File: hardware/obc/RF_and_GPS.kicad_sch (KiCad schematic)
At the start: 15 parts, among them J602 SMA RA Connector, J603 SMA RA Connector, J604 SMA RA Connector, U102 BMI088, U601 RFM98PW, U602 S1216V8, U603 GP2S1+

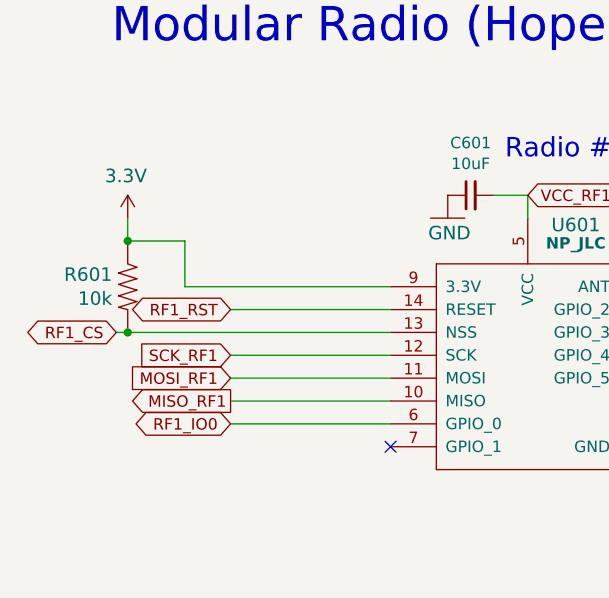
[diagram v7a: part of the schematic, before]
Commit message: OBC: Continuing work towards the next revision
- Cleaned up text on Avionics Page
- Changed some descriptions and cleaned up text on Power Page
- Changed Power Relay A schematic to one from PCB
- Changed R120 and R401 changed from 107k to 34.8k and changed R121 and R404 from 0 to 10k and R127 and R419 from 3.01k to 3.83k (Solar Chargers Page)
- Checked R303 and R304 resistor value and believe 27 is correct
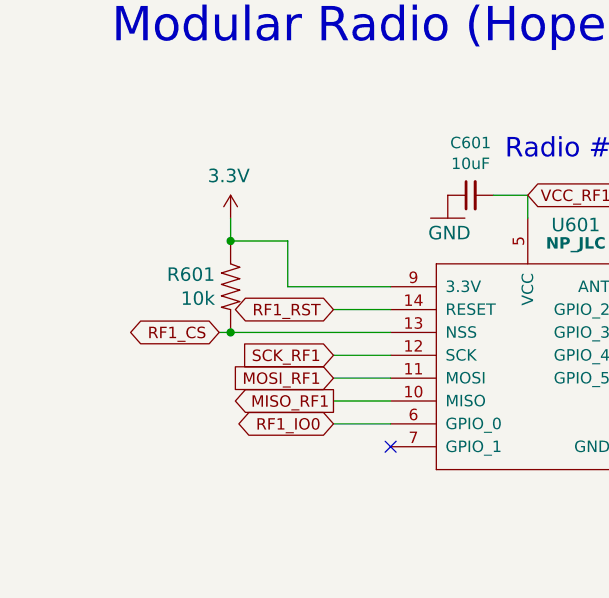
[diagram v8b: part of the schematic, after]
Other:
- moved on the sheet: R601
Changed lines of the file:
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@@
 	)
 	(junction
-		(at 41.91 53.34)
+		(at 53.34 53.34)
 		(diameter 0)
 		(color 0 0 0 0)
@@
 	)
 	(junction
-		(at 41.91 63.5)
+		(at 53.34 63.5)
 		(diameter 0)
 		(color 0 0 0 0)
@@
 	(wire
 		(pts
-			(xy 40.64 63.5) (xy 41.91 63.5)
+			(xy 52.07 63.5) (xy 53.34 63.5)
 		)
 		(stroke
@@
 	(wire
 		(pts
-			(xy 71.12 58.42) (xy 48.26 58.42)
+			(xy 71.12 58.42) (xy 59.69 58.42)
 		)
 		(stroke
@@
 	(wire
 		(pts
-			(xy 48.26 53.34) (xy 41.91 53.34)
-		)
-		(stroke
-			(width 0)
-			(type default)
-		)
-	)
-	(wire
-		(pts
-			(xy 71.12 68.58) (xy 53.34 68.58)
+			(xy 59.69 53.34) (xy 53.34 53.34)
+		)
+		(stroke
+			(width 0)
+			(type default)
+		)
+	)
+	(wire
+		(pts
+			(xy 71.12 68.58) (xy 64.77 68.58)
 		)
 		(stroke
@@
 	(wire
 		(pts
-			(xy 48.26 58.42) (xy 48.26 53.34)
-		)
-		(stroke
-			(width 0)
-			(type default)
-		)
-	)
-	(wire
-		(pts
-			(xy 71.12 71.12) (xy 53.34 71.12)
+			(xy 59.69 58.42) (xy 59.69 53.34)
+		)
+		(stroke
+			(width 0)
+			(type default)
+		)
+	)
+	(wire
+		(pts
+			(xy 71.12 71.12) (xy 64.77 71.12)
 		)
 		(stroke
@@
 	(wire
 		(pts
-			(xy 71.12 60.96) (xy 53.34 60.96)
+			(xy 71.12 60.96) (xy 64.77 60.96)
 		)
 		(stroke
@@
 	(wire
 		(pts
-			(xy 41.91 53.34) (xy 41.91 50.8)
+			(xy 53.34 53.34) (xy 53.34 50.8)
 		)
 		(stroke
@@
 	(wire
 		(pts
-			(xy 41.91 63.5) (xy 71.12 63.5)
+			(xy 53.34 63.5) (xy 71.12 63.5)
 		)
 		(stroke
@@
 	(wire
 		(pts
-			(xy 71.12 66.04) (xy 53.34 66.04)
+			(xy 71.12 66.04) (xy 64.77 66.04)
 		)
 		(stroke
@@
 	(wire
 		(pts
-			(xy 53.34 73.66) (xy 71.12 73.66)
+			(xy 64.77 73.66) (xy 71.12 73.66)
 		)
 		(stroke
@@
 	(global_label "RF1_RST"
 		(shape bidirectional)
-		(at 53.34 60.96 180)
+		(at 64.77 60.96 180)
 		(effects
 			(font
@@
 		)
 		(property "Intersheetrefs" "${INTERSHEET_REFS}"
-			(at 53.34 60.96 0)
+			(at 64.77 60.96 0)
 			(effects
 				(font
@@
 	(global_label "RF1_IO0"
 		(shape bidirectional)
-		(at 53.34 73.66 180)
+		(at 64.77 73.66 180)
 		(effects
 			(font
@@
 		)
 		(property "Intersheetrefs" "${INTERSHEET_REFS}"
-			(at 53.34 73.66 0)
+			(at 64.77 73.66 0)
 			(effects
 				(font
@@
 	(global_label "MOSI_RF1"
 		(shape input)
-		(at 53.34 68.58 180)
+		(at 64.77 68.58 180)
 		(effects
 			(font
@@
 		)
 		(property "Intersheetrefs" "${INTERSHEET_REFS}"
-			(at 53.34 68.58 0)
+			(at 64.77 68.58 0)
 			(effects
 				(font
@@
 	(global_label "RF1_CS"
 		(shape bidirectional)
-		(at 40.64 63.5 180)
+		(at 52.07 63.5 180)
 		(effects
 			(font
@@
 		)
 		(property "Intersheetrefs" "${INTERSHEET_REFS}"
-			(at 40.64 63.5 0)
+			(at 52.07 63.5 0)
 			(effects
 				(font
@@
 	(global_label "SCK_RF1"
 		(shape input)
-		(at 53.34 66.04 180)
+		(at 64.77 66.04 180)
 		(effects
 			(font
@@
 		)
 		(property "Intersheetrefs" "${INTERSHEET_REFS}"
-			(at 53.34 66.04 0)
+			(at 64.77 66.04 0)
 			(effects
 				(font
@@
 	(global_label "MISO_RF1"
 		(shape output)
-		(at 53.34 71.12 180)
+		(at 64.77 71.12 180)
 		(effects
 			(font
@@
 		)
 		(property "Intersheetrefs" "${INTERSHEET_REFS}"
-			(at 53.34 71.12 0)
+			(at 64.77 71.12 0)
 			(effects
 				(font
@@
 	(symbol
 		(lib_id "mainboard:10KOHM-1_10W-1%(0603)0603")
-		(at 41.91 58.42 270)
+		(at 53.34 58.42 270)
 		(unit 1)
 		(exclude_from_sim no)
@@
 		(dnp no)
 		(property "Reference" "R601"
-			(at 40.1828 57.0738 90)
+			(at 51.6128 57.0738 90)
 			(effects
 				(font
@@
 		)
 		(property "Value" "10k"
-			(at 40.1828 59.7408 90)
+			(at 51.6128 59.7408 90)
 			(effects
 				(font
@@
 		)
 		(property "Footprint" "Resistor_SMD:R_0603_1608Metric"
-			(at 41.91 58.42 0)
+			(at 53.34 58.42 0)
 			(effects
 				(font
@@
 		)
 		(property "Datasheet" ""
-			(at 41.91 58.42 0)
+			(at 53.34 58.42 0)
 			(effects
 				(font
@@
 		)
 		(property "Description" "10k 0603"
-			(at 42.7228 57.0738 0)
+			(at 54.1528 57.0738 0)
 			(effects
 				(font
@@
 		)
 		(property "LCSC" "C169849"
-			(at 41.91 58.42 0)
+			(at 53.34 58.42 0)
 			(effects
 				(font
@@
 		)
 		(property "Notes" ""
-			(at 41.91 58.42 0)
+			(at 53.34 58.42 0)
 			(effects
 				(font
@@
 		)
 		(property "Manufacturer_Name" "PANASONIC"
-			(at 41.91 58.42 0)
+			(at 53.34 58.42 0)
 			(effects
 				(font
@@
 		)
 		(property "Manufacturer_Part_Number" "ERJ3GEYJ103V"
-			(at 41.91 58.42 0)
+			(at 53.34 58.42 0)
 			(effects
 				(font
@@
 		)
 		(property "Height" ""
-			(at 41.91 58.42 0)
+			(at 53.34 58.42 0)
 			(effects
 				(font
@@
 		)
 		(property "Mouser Part Number" ""
-			(at 41.91 58.42 0)
+			(at 53.34 58.42 0)
 			(effects
 				(font
@@
 		)
 		(property "Mouser Price/Stock" ""
-			(at 41.91 58.42 0)
+			(at 53.34 58.42 0)
 			(effects
 				(font
@@
 	(symbol
 		(lib_id "mainboard:3.3V")
-		(at 41.91 50.8 0)
+		(at 53.34 50.8 0)
 		(unit 1)
 		(exclude_from_sim no)
@@
 		(dnp no)
 		(property "Reference" "#SUPPLY0601"
-			(at 41.91 50.8 0)
+			(at 53.34 50.8 0)
 			(effects
 				(font
@@
 		)
 		(property "Value" "3.3V"
-			(at 39.37 46.99 0)
+			(at 50.8 46.99 0)
 			(effects
 				(font
@@
 		)
 		(property "Footprint" ""
-			(at 41.91 50.8 0)
+			(at 53.34 50.8 0)
 			(effects
 				(font
@@
 		)
 		(property "Datasheet" ""
-			(at 41.91 50.8 0)
+			(at 53.34 50.8 0)
 			(effects
 				(font
@@
 		)
 		(property "Description" ""
-			(at 41.91 50.8 0)
-			(effects
-				(font
+			(at 53.34 50.8 0)
+			(effects
+				(font
